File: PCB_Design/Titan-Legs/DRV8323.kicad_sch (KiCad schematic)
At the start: 33 parts

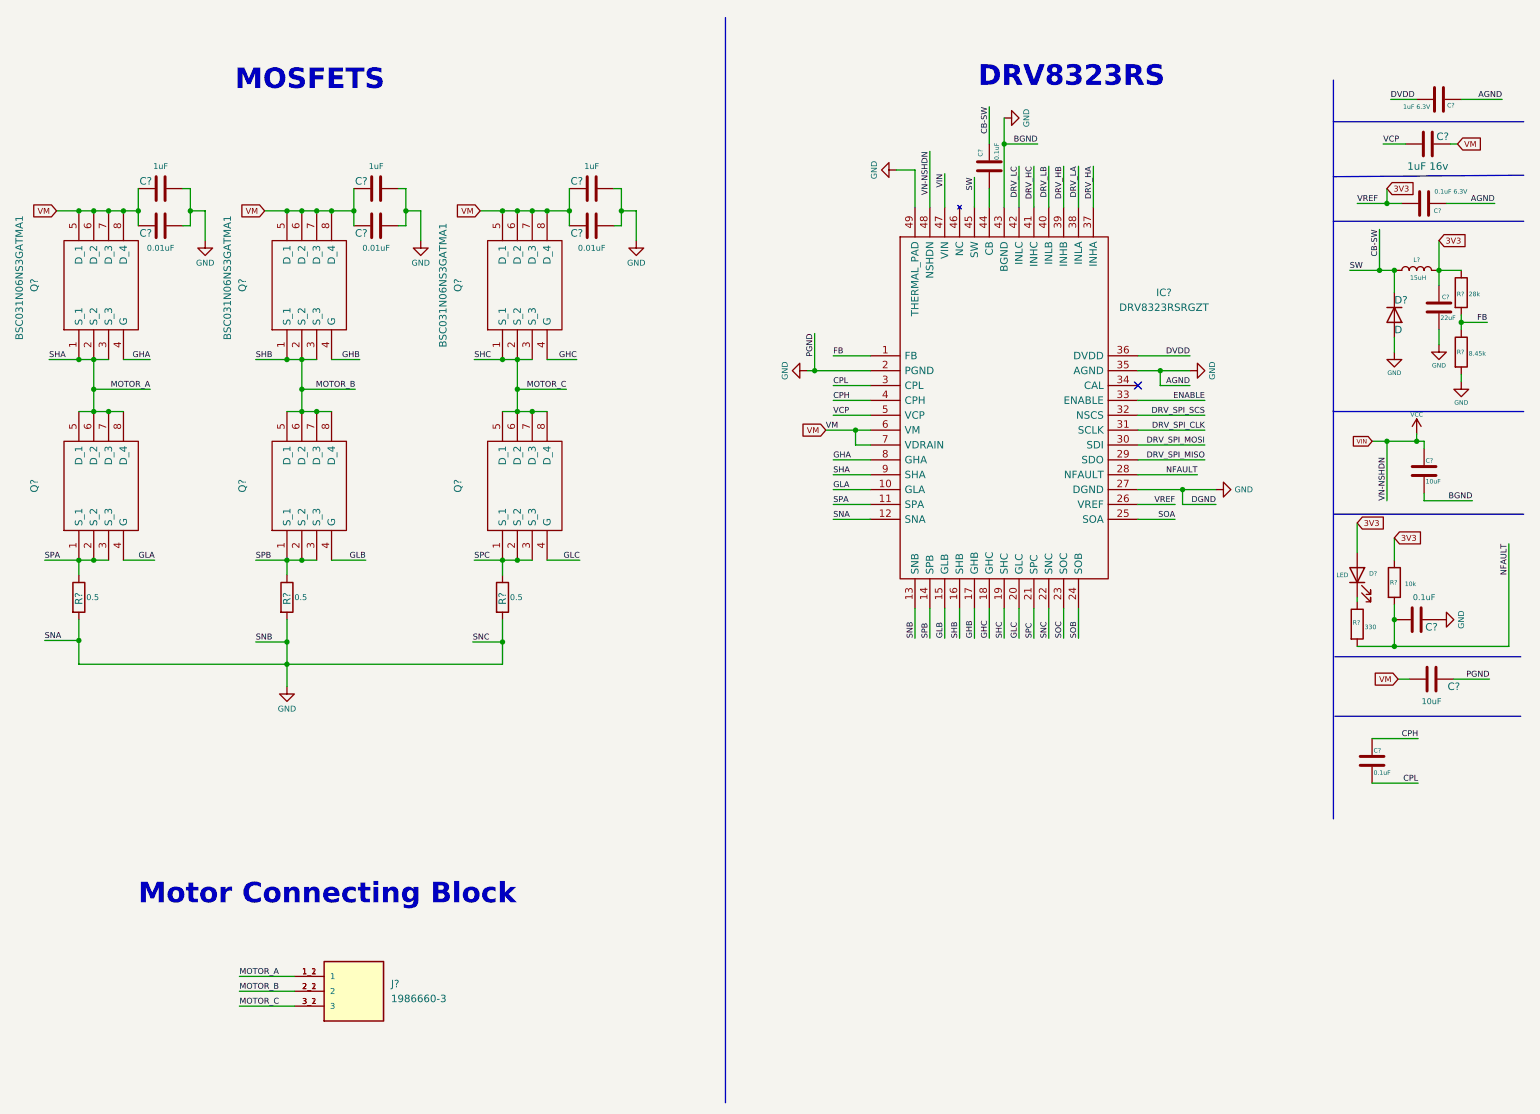
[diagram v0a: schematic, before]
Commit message: schematics 1st iteration completed
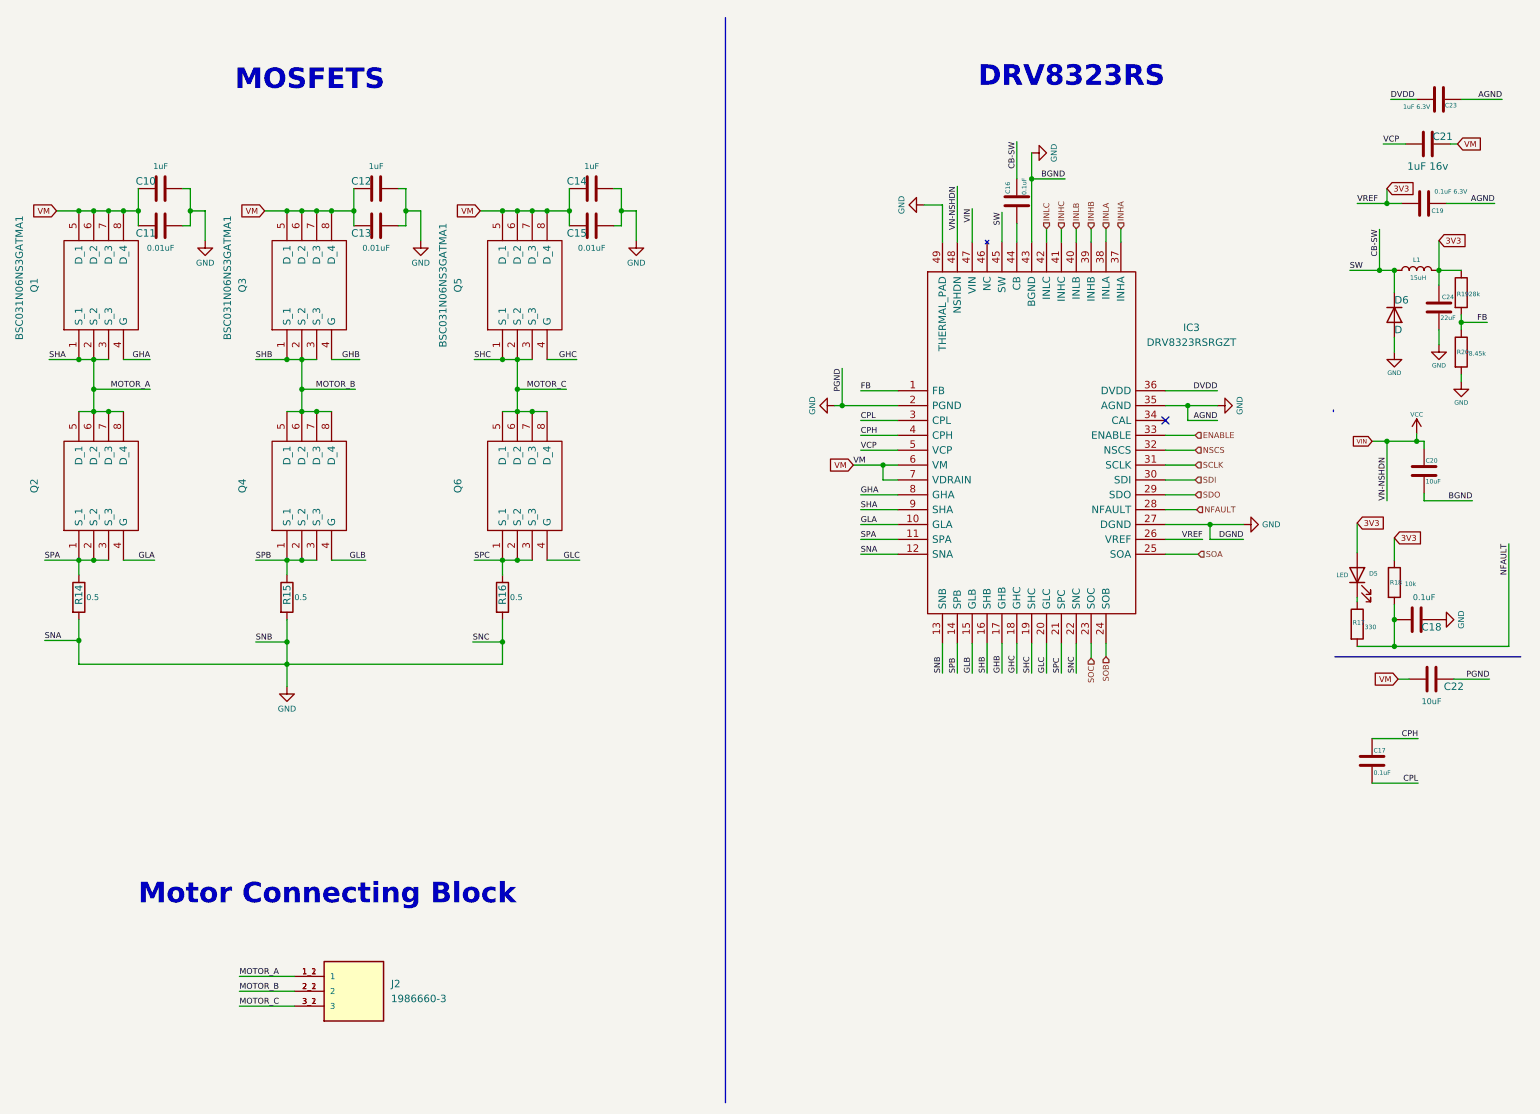
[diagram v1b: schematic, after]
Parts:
- gave numbers to parts that had none: 33
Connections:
- net DRV_HA renamed INHA
- net DRV_HB renamed INHB
- net DRV_HC renamed INHC
- net DRV_LA renamed INLA
- net DRV_LB renamed INLB
- net DRV_LC renamed INLC
- net DRV_SPI_CLK renamed SCLK
- net DRV_SPI_MISO renamed SDO
- net DRV_SPI_MOSI renamed SDI
- net DRV_SPI_SCS renamed NSCS
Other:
- moved on the sheet: C16, IC3

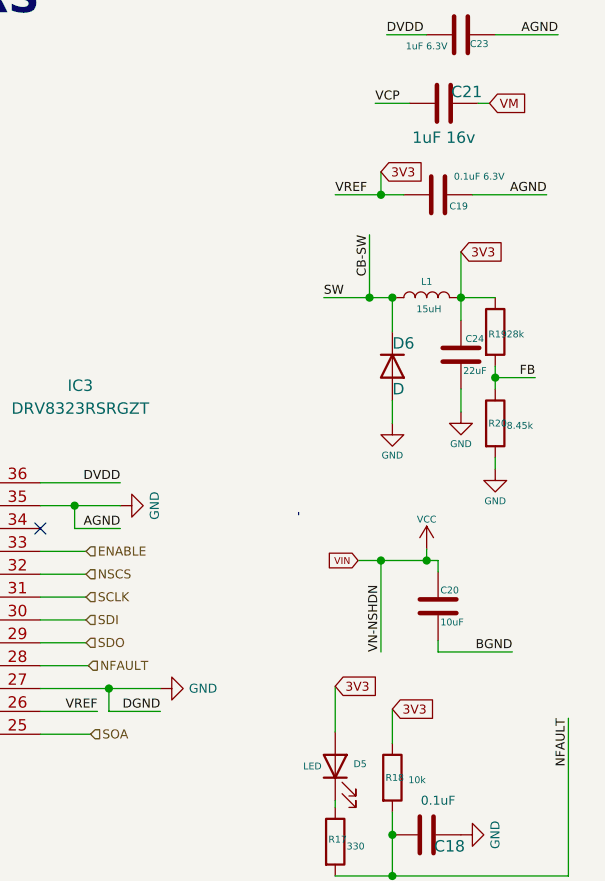
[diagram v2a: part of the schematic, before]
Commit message: Added AMS1117 for ESP32-S3
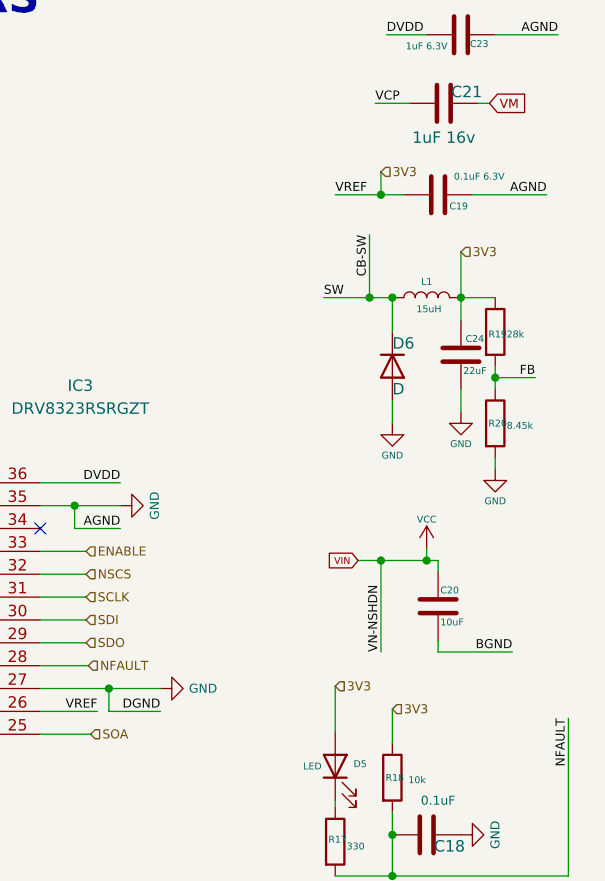
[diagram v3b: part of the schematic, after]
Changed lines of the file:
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@@
-    (stroke (width 0) (type default) (color 0 0 0 0))
-  )
-  (polyline (pts (xy 242.316 80.01) (xy 242.316 79.756))
     (stroke (width 0) (type default) (color 0 0 0 0))
   )
@@
     )
   )
-  (global_label "3V3" (shape input) (at 252.73 101.6 0) (fields_autoplaced)
-    (effects (font (size 1 1)) (justify left))
-    (property "Intersheet References" "${INTERSHEET_REFS}" (id 0) (at 257.3919 101.5375 0)
-      (effects (font (size 1 1)) (justify left) hide)
-    )
-  )
   (global_label "VM" (shape input) (at 263.525 34.29 0) (fields_autoplaced)
     (effects (font (size 1 1)) (justify left))
     (property "Intersheet References" "${INTERSHEET_REFS}" (id 0) (at 267.425 34.2275 0)
-      (effects (font (size 1 1)) (justify left) hide)
-    )
-  )
-  (global_label "3V3" (shape input) (at 251.46 41.91 0) (fields_autoplaced)
-    (effects (font (size 1 1)) (justify left))
-    (property "Intersheet References" "${INTERSHEET_REFS}" (id 0) (at 256.1219 41.8475 0)
-      (effects (font (size 1 1)) (justify left) hide)
-    )
-  )
-  (global_label "3V3" (shape input) (at 246.38 99.06 0) (fields_autoplaced)
-    (effects (font (size 1 1)) (justify left))
-    (property "Intersheet References" "${INTERSHEET_REFS}" (id 0) (at 251.0419 98.9975 0)
       (effects (font (size 1 1)) (justify left) hide)
     )
@@
     )
   )
-  (global_label "3V3" (shape input) (at 260.35 50.8 0) (fields_autoplaced)
-    (effects (font (size 1 1)) (justify left))
-    (property "Intersheet References" "${INTERSHEET_REFS}" (id 0) (at 265.0119 50.7375 0)
-      (effects (font (size 1 1)) (justify left) hide)
-    )
-  )
   (global_label "VM" (shape input) (at 59.69 45.72 180) (fields_autoplaced)
     (effects (font (size 1 1)) (justify right))
@@
     (effects (font (size 1 1)) (justify right))
   )
+  (hierarchical_label "3V3" (shape input) (at 246.38 99.06 0)
+    (effects (font (size 1 1)) (justify left))
+  )
   (hierarchical_label "NSCS" (shape input) (at 218.694 86.614 0)
     (effects (font (size 1 1)) (justify left))
@@
     (effects (font (size 1 1)) (justify left))
   )
+  (hierarchical_label "3V3" (shape input) (at 252.73 101.6 0)
+    (effects (font (size 1 1)) (justify left))
+  )
   (hierarchical_label "NFAULT" (shape input) (at 218.948 96.774 0)
     (effects (font (size 1 1)) (justify left))
   )
+  (hierarchical_label "3V3" (shape input) (at 251.46 41.91 0)
+    (effects (font (size 1 1)) (justify left))
+  )
+  (hierarchical_label "3V3" (shape input) (at 260.35 50.8 0)
+    (effects (font (size 1 1)) (justify left))
+  )

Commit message: updated minor changes
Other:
- moved on the sheet: C17, C18, C19, C20, C21, C22, C23, C24, D5, D6, L1, R17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

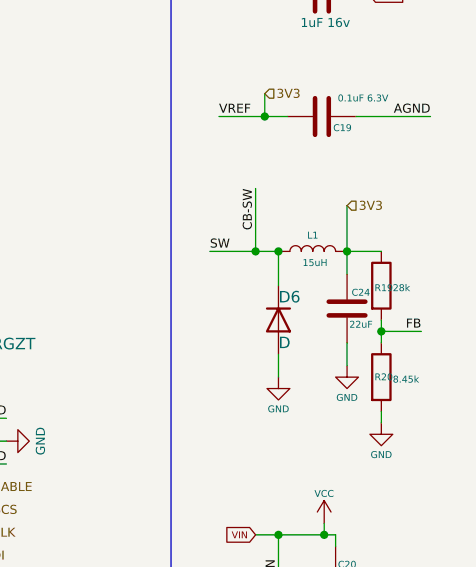
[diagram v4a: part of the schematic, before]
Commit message: added electrolytic capacitors
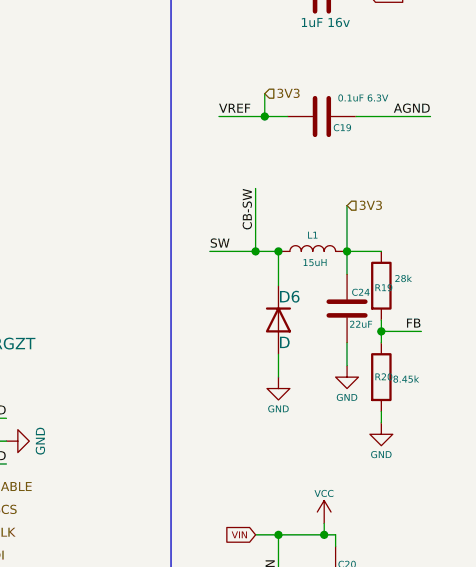
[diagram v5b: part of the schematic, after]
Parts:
- C10, C11, C12, C13, C14, C15, C16, C17, C18, C19, C20, C21, C22, C24: footprint (none) -> Capacitor_SMD:C_0603_1608Metric
- D5: footprint (none) -> LED_SMD:LED_0603_1608Metric
- IC3: footprint QFN50P700X700X100-49N-D -> KiCad:QFN50P700X700X100-49N-D
- J2: footprint TE_1986660-3 -> 3x Terminal Block:TE_1986660-3
- Q1, Q2, Q3, Q4, Q5, Q6: footprint PG-TDSON-8_1 -> BSC_Mosfets:PG-TDSON-8_1
- R18: footprint (none) -> Resistor_SMD:R_0603_1608Metric
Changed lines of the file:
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@@
       (effects (font (size 0.762 0.762)) (justify right))
     )
-    (property "Footprint" "" (id 2) (at 252.5268 152.4 0)
+    (property "Footprint" "Capacitor_SMD:C_0603_1608Metric" (id 2) (at 252.5268 152.4 0)
       (effects (font (size 1.27 1.27)) hide)
     )
@@
       (effects (font (size 1 1)))
     )
-    (property "Footprint" "" (id 2) (at 82.55 40.9448 0)
+    (property "Footprint" "Capacitor_SMD:C_0603_1608Metric" (id 2) (at 82.55 40.9448 0)
       (effects (font (size 1.27 1.27)) hide)
     )
@@
     (property "Reference" "Q3" (id 0) (at 55.88 58.42 0))
     (property "Value" "BSC031N06NS3GATMA1" (id 1) (at 53.34 57.15 0))
-    (property "Footprint" "PG-TDSON-8_1" (id 2) (at 60.96 49.53 0)
+    (property "Footprint" "BSC_Mosfets:PG-TDSON-8_1" (id 2) (at 60.96 49.53 0)
       (effects (font (size 1.27 1.27)) (justify left) hide)
     )
@@
       (effects (font (size 0.762 0.762)) (justify right))
     )
-    (property "Footprint" "" (id 2) (at 246.634 116.078 0)
+    (property "Footprint" "LED_SMD:LED_0603_1608Metric" (id 2) (at 246.634 116.078 0)
       (effects (font (size 1.27 1.27)) hide)
     )
@@
     (property "Reference" "IC3" (id 0) (at 218.059 65.659 0))
     (property "Value" "DRV8323RSRGZT" (id 1) (at 218.059 68.199 0))
-    (property "Footprint" "QFN50P700X700X100-49N-D" (id 2) (at 209.804 56.134 0)
+    (property "Footprint" "KiCad:QFN50P700X700X100-49N-D" (id 2) (at 209.804 56.134 0)
       (effects (font (size 1.27 1.27)) (justify left) hide)
     )
@@
       (effects (font (size 0.762 0.762)) (justify left))
     )
-    (property "Value" "28k" (id 1) (at 265.43 61.976 0)
+    (property "Value" "28k" (id 1) (at 265.6332 60.96 0)
       (effects (font (size 0.762 0.762)) (justify left))
     )
@@
       (effects (font (size 1.27 1.27)) hide)
     )
-    (property "Footprint" "PG-TDSON-8_1" (id 2) (at 60.96 83.82 0)
+    (property "Footprint" "BSC_Mosfets:PG-TDSON-8_1" (id 2) (at 60.96 83.82 0)
       (effects (font (size 1.27 1.27)) (justify left) hide)
     )
@@
       (effects (font (size 1 1)))
     )
-    (property "Footprint" "" (id 2) (at 45.72 47.2948 0)
+    (property "Footprint" "Capacitor_SMD:C_0603_1608Metric" (id 2) (at 45.72 47.2948 0)
       (effects (font (size 1.27 1.27)) hide)
     )
@@
       (effects (font (size 1 1)))
     )
-    (property "Footprint" "" (id 2) (at 260.604 122.7328 0)
+    (property "Footprint" "Capacitor_SMD:C_0603_1608Metric" (id 2) (at 260.604 122.7328 0)
       (effects (font (size 1.27 1.27)) hide)
     )
@@
       (effects (font (size 0.762 0.762)) (justify left))
     )
-    (property "Footprint" "" (id 2) (at 251.206 117.348 90)
+    (property "Footprint" "Resistor_SMD:R_0603_1608Metric" (id 2) (at 251.206 117.348 90)
       (effects (font (size 1.27 1.27)) hide)
     )
@@
       (effects (font (size 1 1)))
     )
-    (property "Footprint" "" (id 2) (at 45.72 40.9448 0)
+    (property "Footprint" "Capacitor_SMD:C_0603_1608Metric" (id 2) (at 45.72 40.9448 0)
       (effects (font (size 1.27 1.27)) hide)
     )
@@
       (effects (font (size 1 1)))
     )
-    (property "Footprint" "" (id 2) (at 261.366 138.4808 0)
+    (property "Footprint" "Capacitor_SMD:C_0603_1608Metric" (id 2) (at 261.366 138.4808 0)
       (effects (font (size 1.27 1.27)) hide)
     )
@@
       (effects (font (size 1 1)))
     )
-    (property "Footprint" "" (id 2) (at 119.38 40.9448 0)
+    (property "Footprint" "Capacitor_SMD:C_0603_1608Metric" (id 2) (at 119.38 40.9448 0)
       (effects (font (size 1.27 1.27)) hide)
     )
@@
       (effects (font (size 0.762 0.762)))
     )
-    (property "Footprint" "" (id 2) (at 261.366 41.9608 0)
+    (property "Footprint" "Capacitor_SMD:C_0603_1608Metric" (id 2) (at 261.366 41.9608 0)
       (effects (font (size 1.27 1.27)) hide)
     )
@@
       (effects (font (size 0.762 0.762)))
     )
-    (property "Footprint" "" (id 2) (at 187.2488 40.259 0)
+    (property "Footprint" "Capacitor_SMD:C_0603_1608Metric" (id 2) (at 187.2488 40.259 0)
       (effects (font (size 1.27 1.27)) hide)
     )
@@
     (property "Reference" "Q5" (id 0) (at 92.71 58.42 0))
     (property "Value" "BSC031N06NS3GATMA1" (id 1) (at 90.17 58.42 0))
-    (property "Footprint" "PG-TDSON-8_1" (id 2) (at 97.79 49.53 0)
+    (property "Footprint" "BSC_Mosfets:PG-TDSON-8_1" (id 2) (at 97.79 49.53 0)
       (effects (font (size 1.27 1.27)) (justify left) hide)
     )
@@
       (effects (font (size 1 1)))
     )
-    (property "Footprint" "" (id 2) (at 261.366 28.2448 0)
+    (property "Footprint" "Capacitor_SMD:C_0603_1608Metric" (id 2) (at 261.366 28.2448 0)
       (effects (font (size 1.27 1.27)) hide)
     )
@@
     (property "Reference" "Q1" (id 0) (at 20.32 58.42 0))
     (property "Value" "BSC031N06NS3GATMA1" (id 1) (at 17.78 57.15 0))
-    (property "Footprint" "PG-TDSON-8_1" (id 2) (at 25.4 49.53 0)
+    (property "Footprint" "BSC_Mosfets:PG-TDSON-8_1" (id 2) (at 25.4 49.53 0)
       (effects (font (size 1.27 1.27)) (justify left) hide)
     )
@@
       (effects (font (size 1 1)))
     )
-    (property "Footprint" "" (id 2) (at 119.38 47.2948 0)
+    (property "Footprint" "Capacitor_SMD:C_0603_1608Metric" (id 2) (at 119.38 47.2948 0)
       (effects (font (size 1.27 1.27)) hide)
     )
@@
       (effects (font (size 1.27 1.27)) (justify left))
     )
-    (property "Footprint" "TE_1986660-3" (id 2) (at 74.93 179.07 0)
+    (property "Footprint" "3x Terminal Block:TE_1986660-3" (id 2) (at 74.93 179.07 0)
       (effects (font (size 1.27 1.27)) (justify bottom) hide)
     )
@@
       (effects (font (size 1.27 1.27)) hide)
     )
-    (property "Footprint" "PG-TDSON-8_1" (id 2) (at 25.4 83.82 0)
+    (property "Footprint" "BSC_Mosfets:PG-TDSON-8_1" (id 2) (at 25.4 83.82 0)
       (effects (font (size 1.27 1.27)) (justify left) hide)
     )
@@
       (effects (font (size 1.27 1.27)) hide)
     )
-    (property "Footprint" "PG-TDSON-8_1" (id 2) (at 97.79 83.82 0)
+    (property "Footprint" "BSC_Mosfets:PG-TDSON-8_1" (id 2) (at 97.79 83.82 0)
       (effects (font (size 1.27 1.27)) (justify left) hide)
     )
@@
       (effects (font (size 0.762 0.762)) (justify left))
     )
-    (property "Footprint" "" (id 2) (at 260.0452 98.298 0)
+    (property "Footprint" "Capacitor_SMD:C_0603_1608Metric" (id 2) (at 260.0452 98.298 0)
       (effects (font (size 1.27 1.27)) hide)
     )
@@
       (effects (font (size 0.762 0.762)) (justify left))
     )
-    (property "Footprint" "" (id 2) (at 261.3152 68.072 0)
+    (property "Footprint" "Capacitor_SMD:C_0603_1608Metric" (id 2) (at 261.3152 68.072 0)
       (effects (font (size 1.27 1.27)) hide)
     )
@@
       (effects (font (size 1 1)))
     )
-    (property "Footprint" "" (id 2) (at 82.55 47.2948 0)
-      (effects (font (size 1.27 1.27)) hide)
-    )
+    (property "Footprint" "Capacitor_SMD:C_0603_1608Metric" (id 2) (at 82.55 47.2948 0)
+      (effects (font (size 1.27 1.27)) hide)
+    )

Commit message: footprint assignment done
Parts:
- removed C16: 0.1uF, Capacitor_SMD:C_0603_1608Metric, symbol Device:C
- removed C20: 10uF, Capacitor_SMD:C_0603_1608Metric, symbol Device:C
- removed C24: 22uF, Capacitor_SMD:C_0603_1608Metric, symbol Device:C
- removed D6: D, symbol Device:D
- removed L1: 15uH, symbol Device:L
- removed R19: 28k, symbol Device:R
- removed R20: 8.45k, symbol Device:R
- R14, R15, R16: value 0.5 -> 0.5m; footprint (none) -> 3x Terminal Block:0.5m_resistor
- R17: footprint (none) -> Resistor_SMD:R_0603_1608Metric
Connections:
- net CB-SW: no longer names the net of IC3.45 (SW)
- net FB: no longer names the net of IC3.1 (FB)
- net VCC: no longer names the net of IC3.47 (VIN)
- net VCC: no longer IC3.48 (NSHDN)
- no-connect marks 1 -> 6
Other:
- moved on the sheet: C17, C18, C19, C21, C22, C23, D5, R17, R18
